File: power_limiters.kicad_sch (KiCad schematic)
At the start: 30 parts, among them U10 MAX4995AAUT+T, U11 MAX4995AAUT+T, U26 SN74AHC1G08QDCKRQ1, U35 MAX4995AAUT+T, U8 MPQ5072GG-AEC1-Z, U9 MAX4995AAUT+T

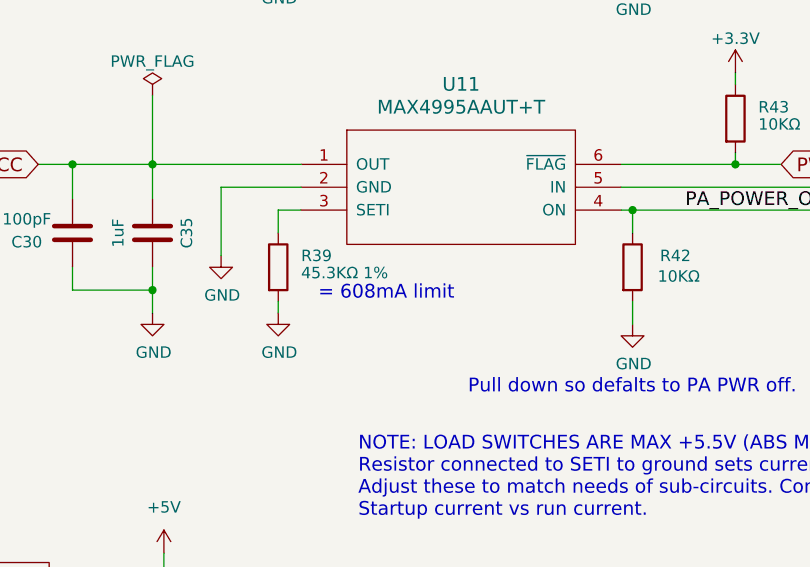
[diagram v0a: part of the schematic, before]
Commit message: Change PA power limit to 630ma
Need a little bit more power.

Signed-off-by: Corey Minyard <corey@minyard.net>
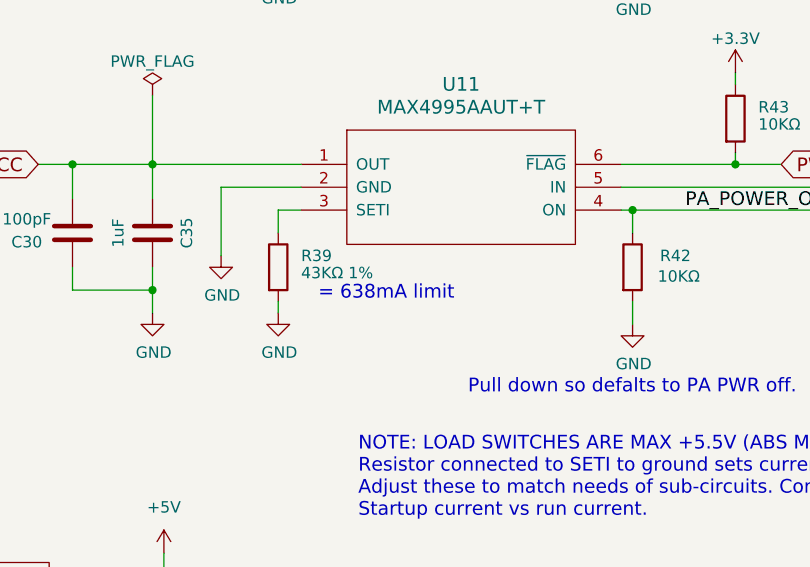
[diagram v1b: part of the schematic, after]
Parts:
- R39: value 45.3KΩ 1% -> 43KΩ 1%
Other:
- note added: "= 638mA limit"
- note removed: "= 608mA limit"
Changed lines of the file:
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@@
 		)
 	)
-	(text "= 608mA limit"
+	(text "= 638mA limit"
 		(exclude_from_sim no)
 		(at 180.975 132.08 0)
@@
 			)
 		)
-		(property "Value" "45.3KΩ 1%"
+		(property "Value" "43KΩ 1%"
 			(at 179.07 128.905 0)
 			(effects
